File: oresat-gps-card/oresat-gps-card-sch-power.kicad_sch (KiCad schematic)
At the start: 95 parts, among them Q1 DMP2240UDM, Q2 PMV45EN, Q3 DMP3050LVT-7, Q4 DMP3050LVT-7, Q5 PMV45EN, U2 MAX7310ATE, U3 MIC842LYC5, U4 MIC842LYC5, U5 MAX4211FETE, U6 LTC3624, U7 TS5A21366

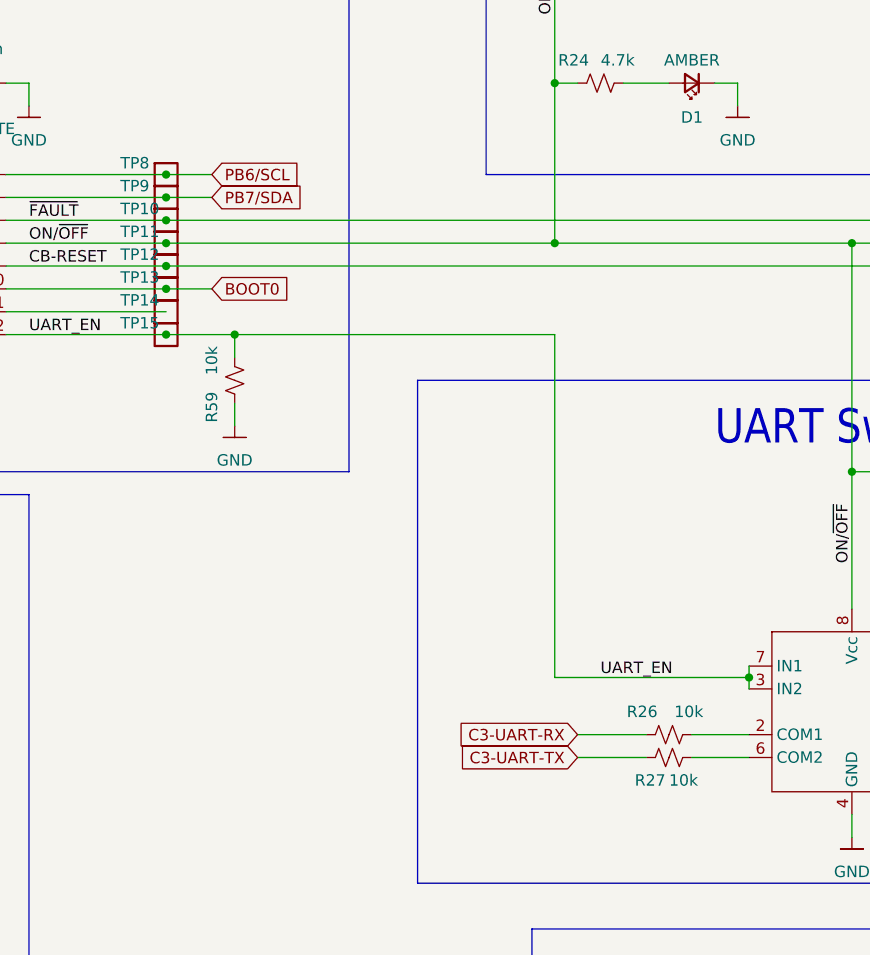
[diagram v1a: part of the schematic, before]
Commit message: Quick GPS card design review changes
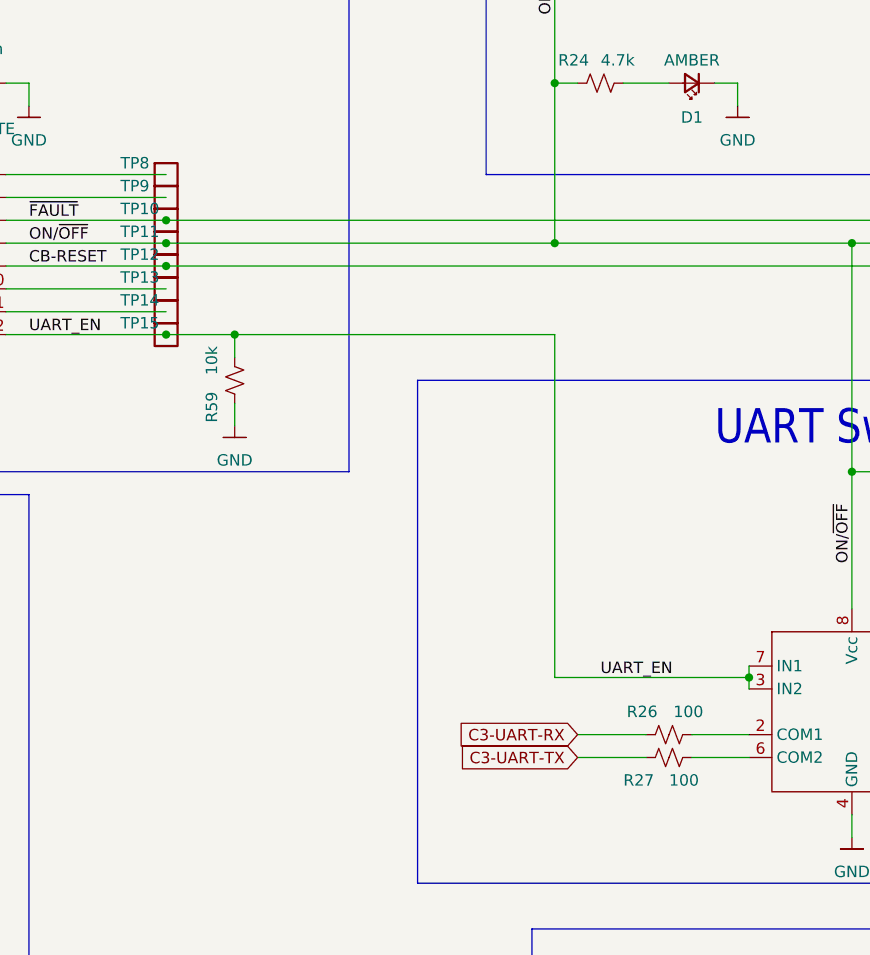
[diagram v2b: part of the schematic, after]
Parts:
- R26, R27: value 10k -> 100
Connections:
- net BOOT0: no longer names the net of TP13.1, U2.10 (IO5)
- net PB6/SCL: no longer names the net of TP8.1, U2.4 (IO0)
- net PB7/SDA: no longer names the net of TP9.1, U2.5 (IO1)

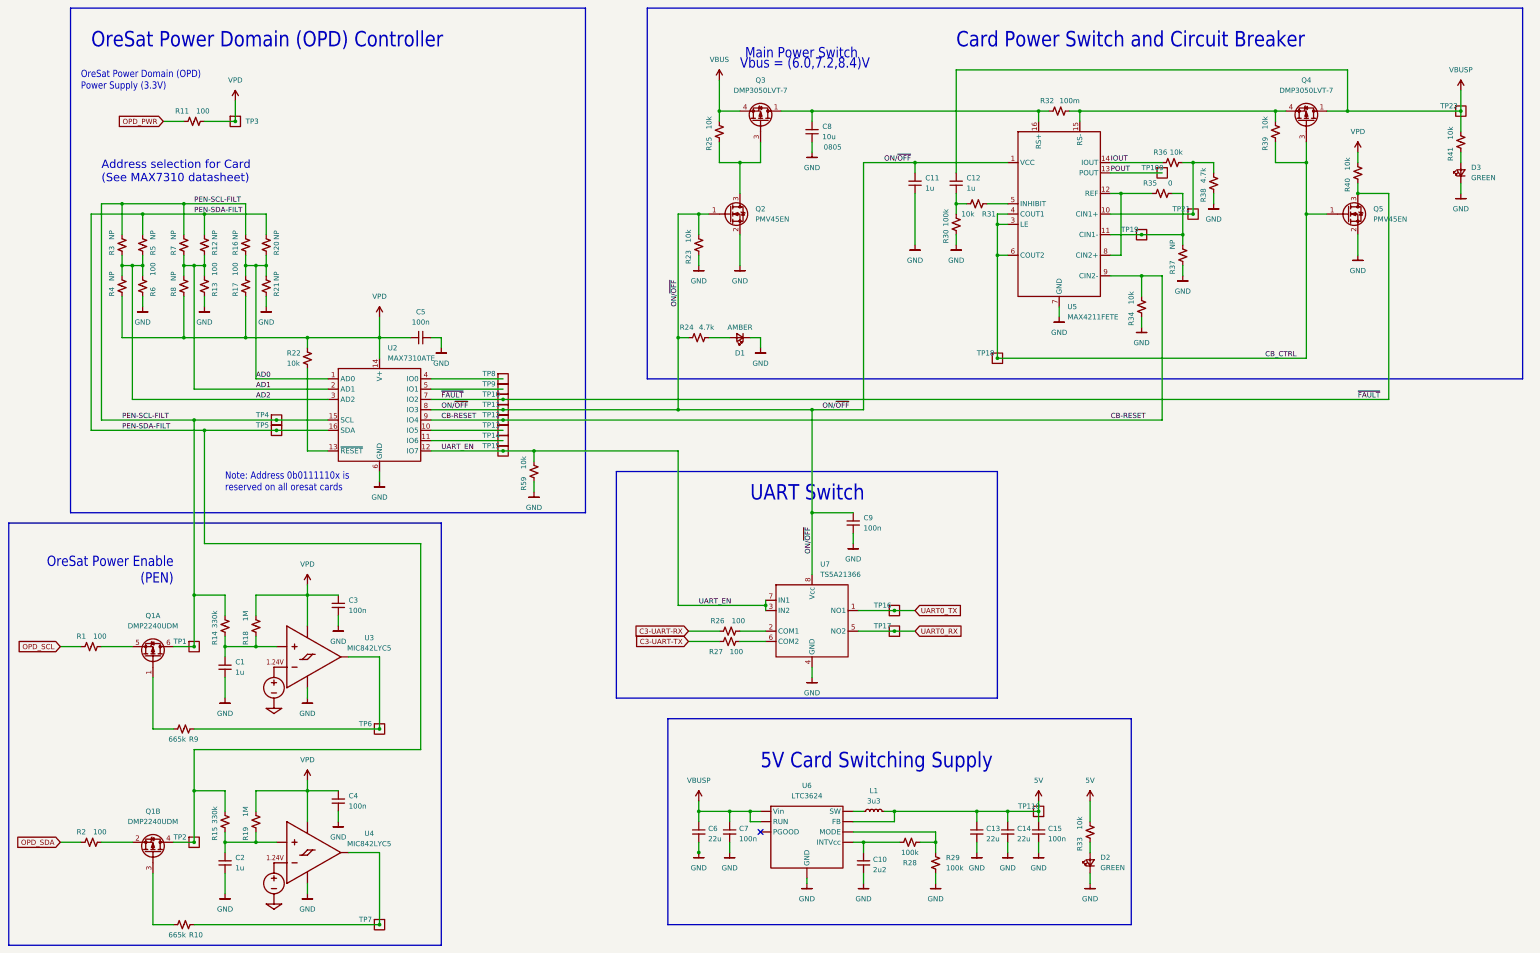
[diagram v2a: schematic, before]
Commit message: Updated GPS card with changes from C3 and notes. Fixed library issues
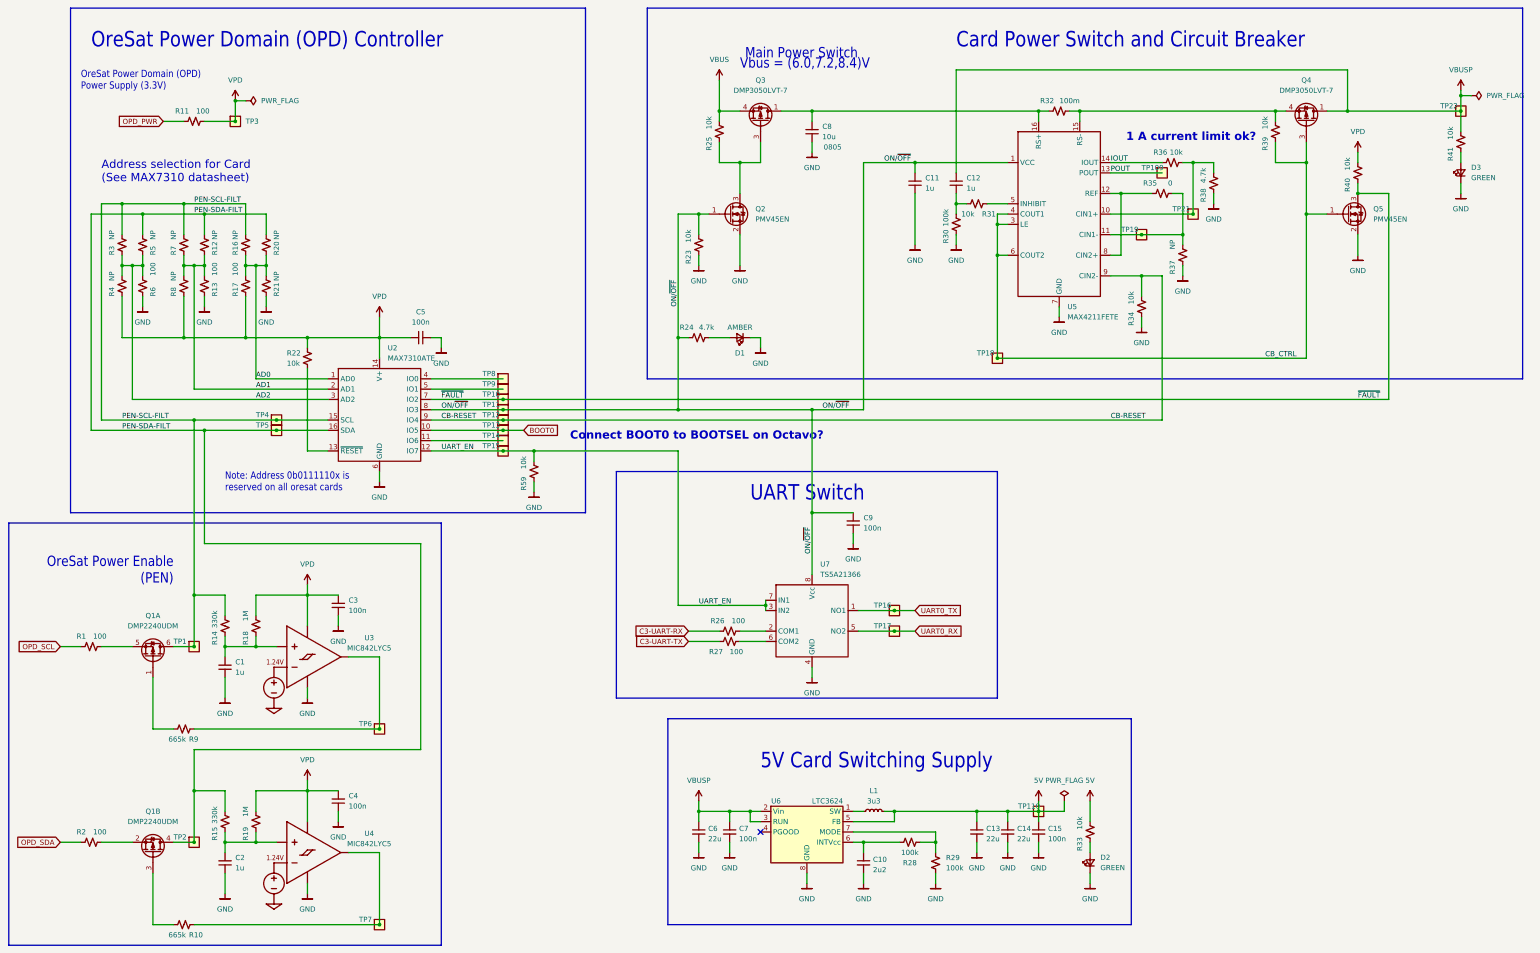
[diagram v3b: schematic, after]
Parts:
- Q3, Q4: symbol Q-DiodesInc-DMP3050LVT-PCH-Mosfet:DMP3050LVT-7 -> oresat-transistors:DMP3050LVT-7
- TP1, TP10, TP109, TP11, TP110, TP12, TP13, TP14, TP15, TP16, TP17, TP18, TP19, TP2, TP21, TP22, TP3, TP4, TP5, TP6, TP7, TP8, TP9: value Test-Point -> 1x01; footprint OreSat-TestPoint:1X01 -> oresat-misc:TestPoint-0.75mm-th; symbol OreSat-TestPoint:Test-Point -> oresat-misc:Test-Point-0.75mm-th
- U2: symbol U-Maxim-MAX7310-I2C-GPIO-expander:MAX7310 -> oresat-ics:MAX7310
- U3, U4: symbol U-Microchip-MIC842-Comparator:MIC842LYC5 -> oresat-ics:MIC842LYC5
- U5: symbol U-Maxim-MAX4211-power-monitor:MAX4211FETE -> oresat-ics:MAX4211FETE
- U6: footprint oresat-footprints:DFN-8-1EP_3x3mm_P0.5mm_EP1.65x2.38mm_ThermalVias0.3mm -> oresat-ics:DFN-8-1EP_3x3mm_P0.5mm_EP1.65x2.38mm_ThermalVias0.3mm; symbol U-Linear Tech-LTC3624:LTC3624 -> oresat-ics:LTC3624
- U7: symbol U-TI-TS5A21366-2xSPST-analog-switch:TS5A21366 -> oresat-ics:TS5A21366
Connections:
- net BOOT0: now reaches TP13.1, U2.10 (IO5)
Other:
- note added: "1 A current limit ok?"
- note added: "Connect BOOT0 to BOOTSEL on Octavo?"

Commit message: Updated GPS card
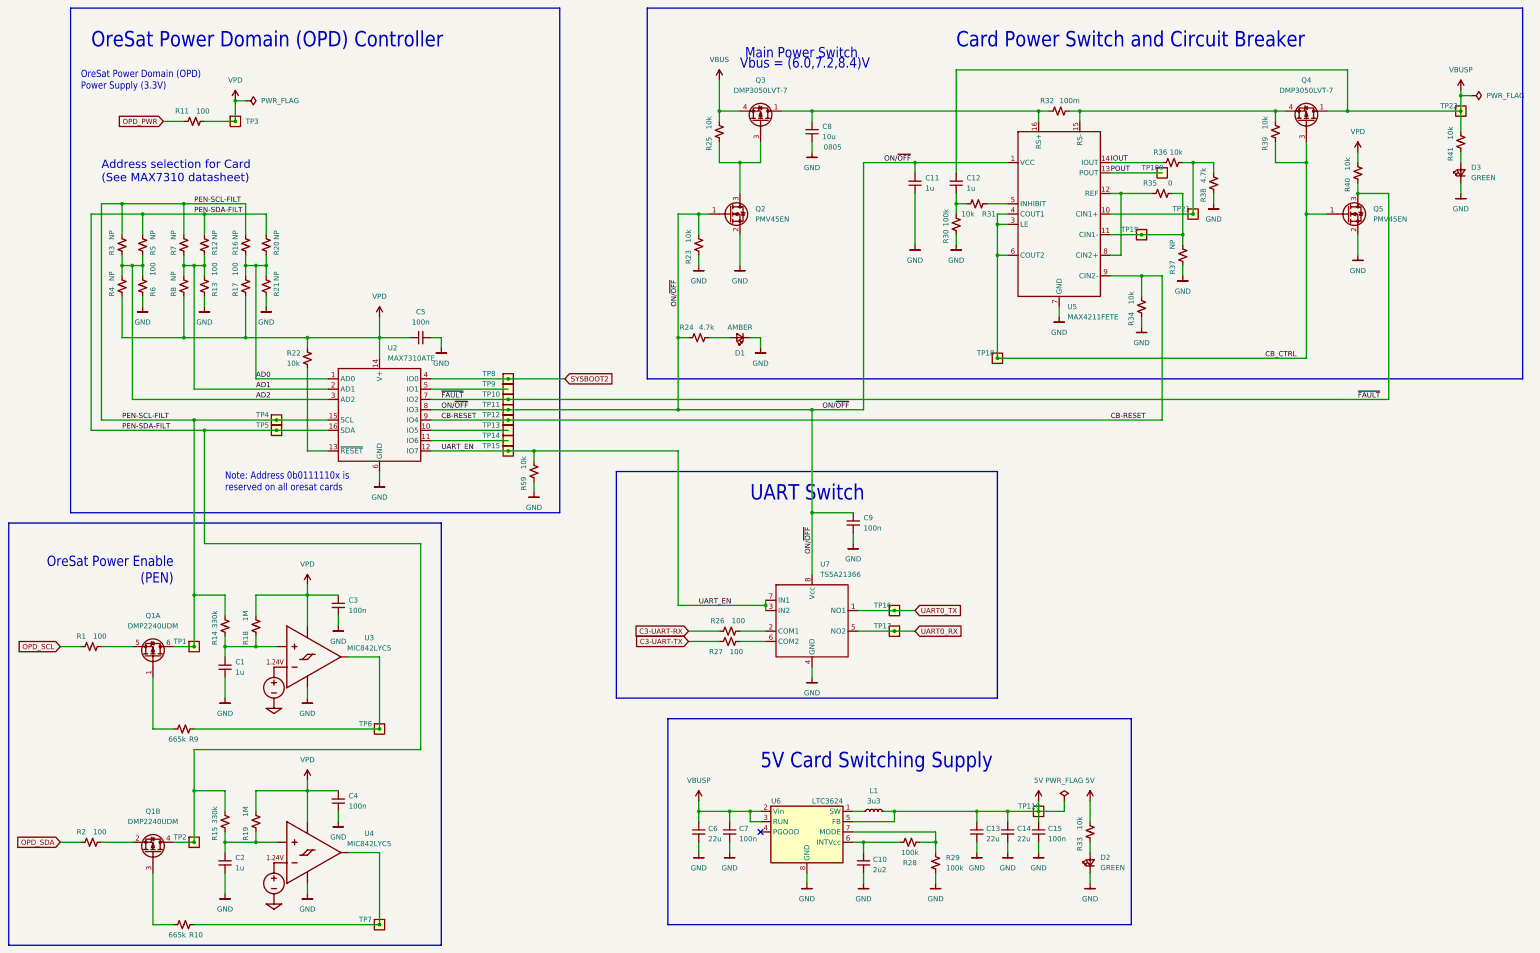
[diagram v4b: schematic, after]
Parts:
- L1: footprint oresat-footprints:L_ECS-MPI4040 -> oresat-passives:L_ECS-MPI4040
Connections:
- net SYSBOOT2: now reaches TP8.1, U2.4 (IO0)
- net BOOT0: no longer names the net of TP13.1, U2.10 (IO5)
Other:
- note removed: "1 A current limit ok?"
- note removed: "Connect BOOT0 to BOOTSEL on Octavo?"
- moved on the sheet: TP10, TP11, TP12, TP13, TP14, TP15, TP8, TP9
